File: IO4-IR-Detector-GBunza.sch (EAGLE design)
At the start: 45 parts, among them CON2 IO4INV, IC1 TL331, IC2 TL331, IC3 TL331, IC4 TL331, Q1 2N7002, Q2 2N7002, Q3 2N7002, Q4 2N7002

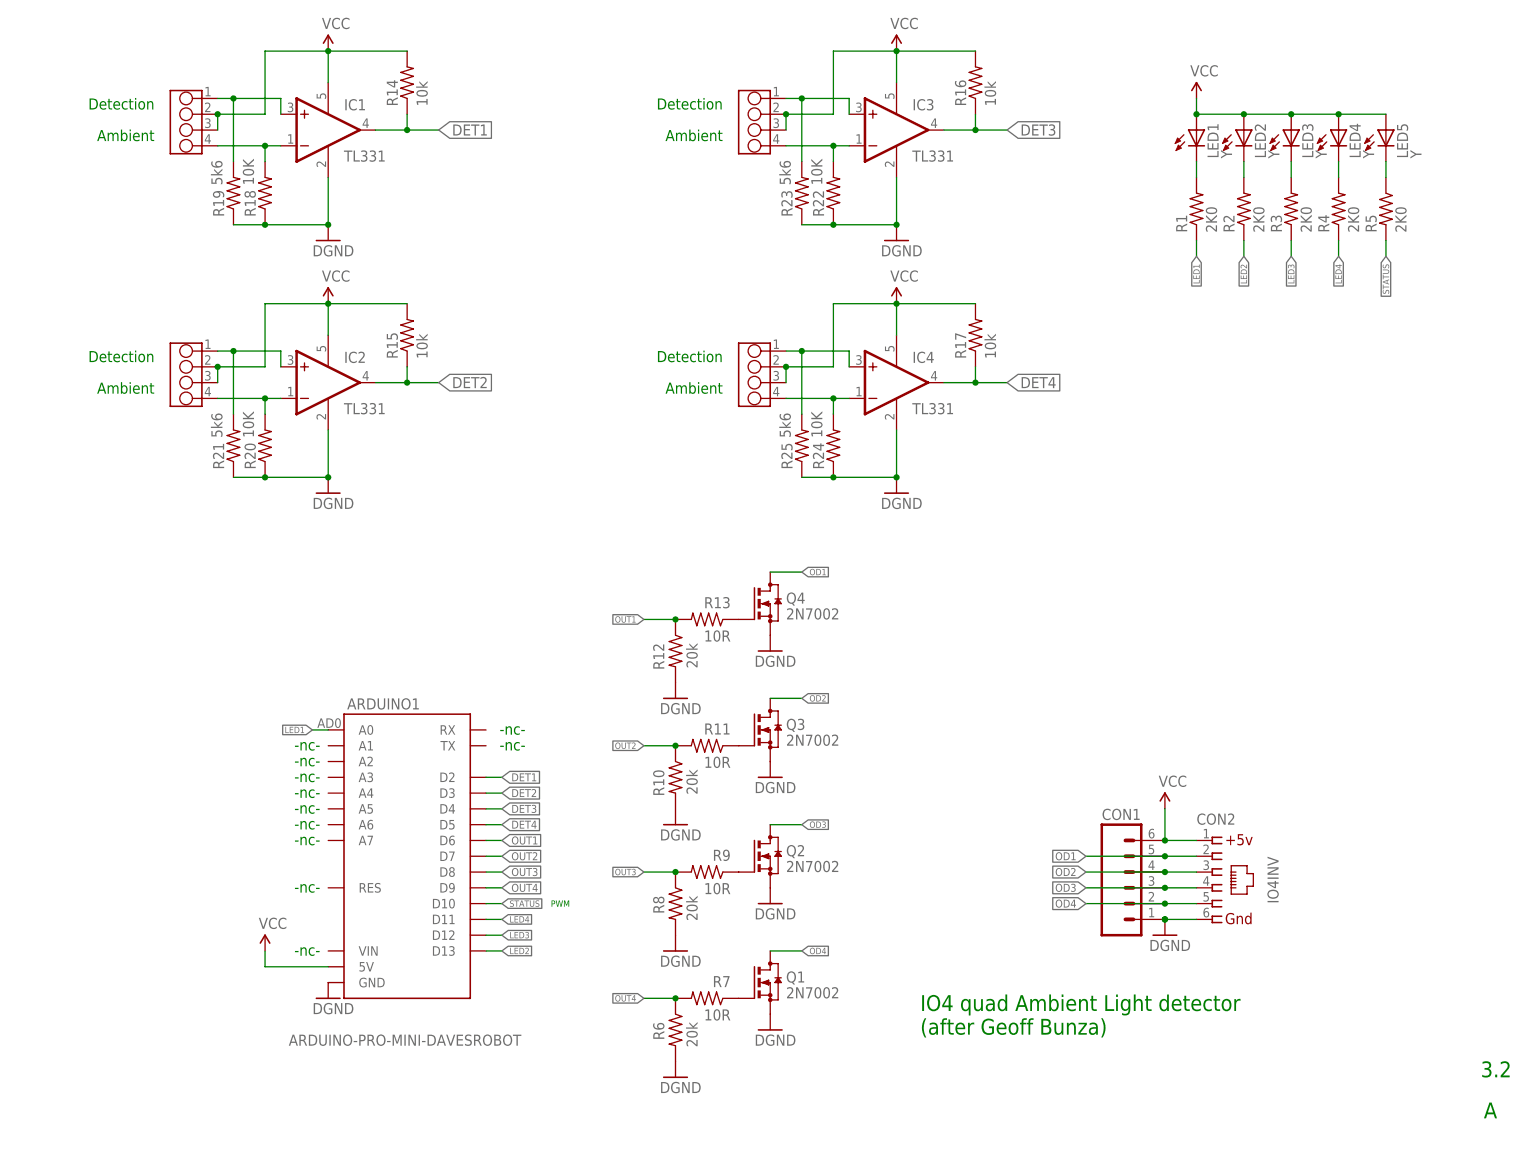
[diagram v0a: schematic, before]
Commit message: changed from expensive TL331 to inexpensive LM258/LM358
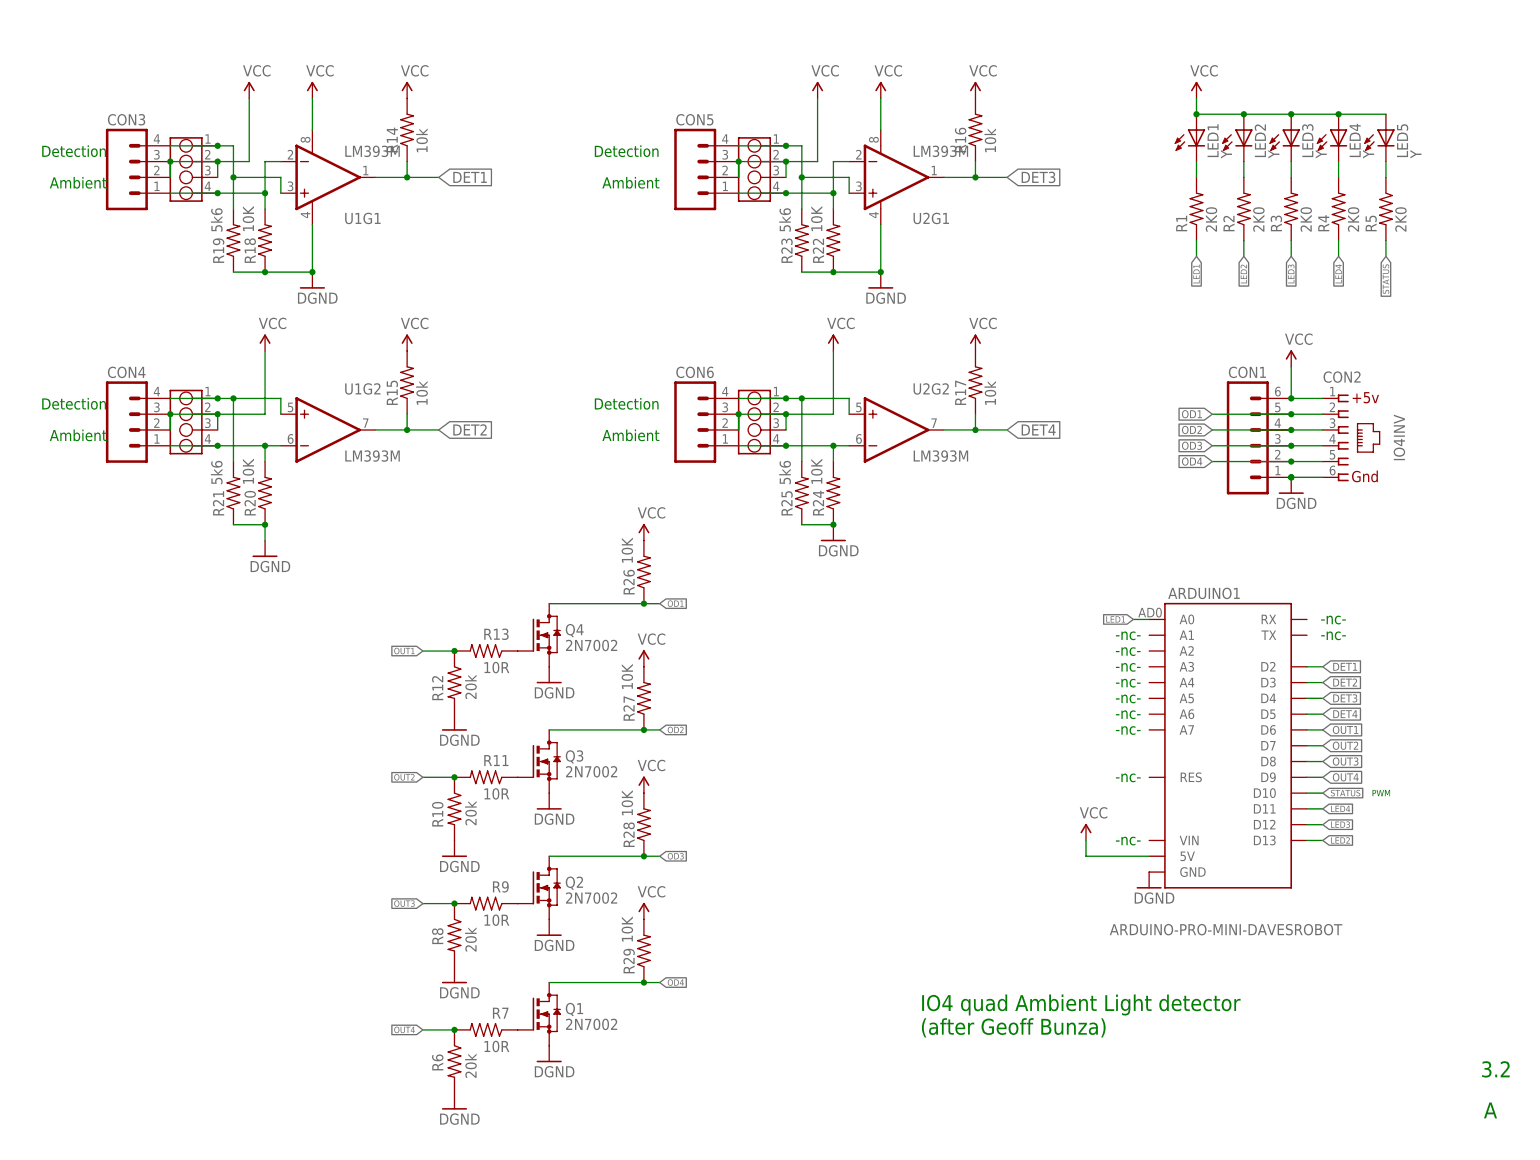
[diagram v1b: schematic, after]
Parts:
- removed IC1, IC2, IC3, IC4: TL331, SPCoast:TL331
- added CON3, CON4, CON5, CON6: (no value), SPCoast:CONNECTOR-M04LOCK
- added R26, R27, R28, R29: 10K, SPCoast:R0805-RES
- added U1, U2: LM393M, SPCoast:LM393M
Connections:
- net DET1: now also U1G1.OUT; no longer IC1.OUT
- net DET2: now also U1G2.OUT; no longer IC2.OUT
- net DET3: now also U2G1.OUT; no longer IC3.OUT
- net DET4: now also U2G2.OUT; no longer IC4.OUT
- net GND: now also U1G1.V-, U2G1.V-; no longer IC1.GND, IC2.GND, IC3.GND, IC4.GND
- net N$10: now also CON4.1, U1G2.-IN; no longer IC2.-IN
- net N$12: now also CON4.4, U1G2.+IN; no longer IC2.+IN
- net N$13: now also CON5.1, U2G1.-IN; no longer IC3.-IN
- net N$14: now also CON5.4, U2G1.+IN; no longer IC3.+IN
- net N$15: now also CON6.1, U2G2.-IN; no longer IC4.-IN
- net N$16: now also CON6.4, U2G2.+IN; no longer IC4.+IN
- net N$19: now also CON3.4, U1G1.+IN; no longer IC1.+IN
- net N$9: now also CON3.1, U1G1.-IN; no longer IC1.-IN
- net OD1: now also R26.1
- net OD2: now also R27.1
- net OD3: now also R28.1
- net OD4: now also R29.1
- net VCC: now also CON3.2, CON3.3, CON4.2, CON4.3, CON5.2, CON5.3, CON6.2, CON6.3, R26.2, R27.2, R28.2, R29.2, U1G1.V+, U2G1.V+; no longer IC1.V+, IC2.V+, IC3.V+, IC4.V+
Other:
- moved on the sheet: ARDUINO1, CON1, CON2, Q1, Q2, Q3, Q4, R10, R11, R12, R13, R14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

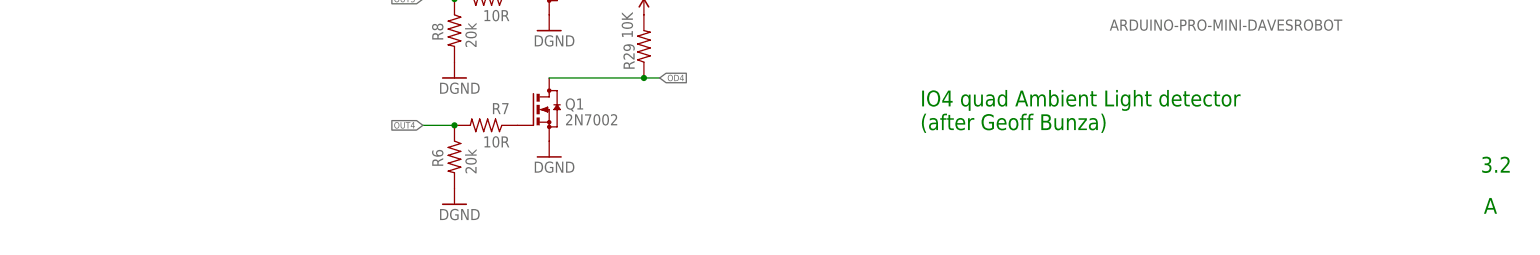
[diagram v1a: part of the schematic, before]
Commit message: added V4 changes note to sch
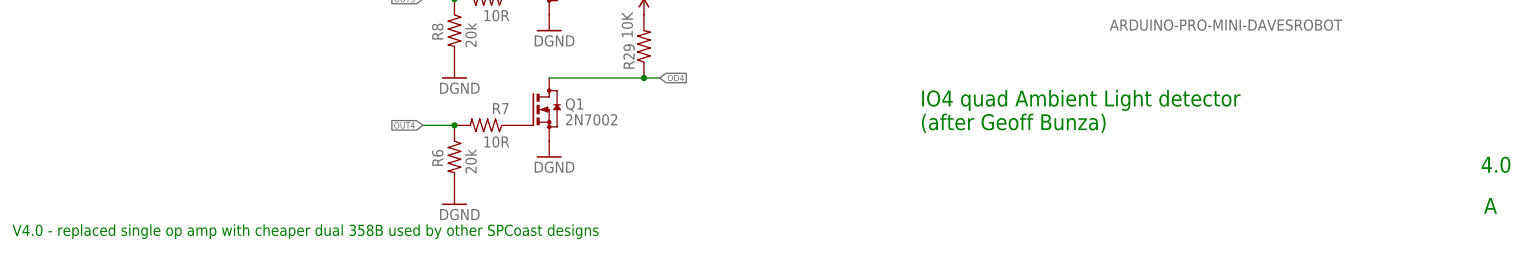
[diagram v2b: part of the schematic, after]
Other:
- note added: "4.0"
- note added: "V4.0 - replaced single op amp with cheaper dual 358B used by other SPCoast designs"
- note removed: "3.2"
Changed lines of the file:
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@@
 <text x="151.13" y="19.558" size="2.54" layer="91">IO4 quad Ambient Light detector
 (after Geoff Bunza)</text>
-<text x="241.3" y="12.7" size="2.54" layer="91">3.2</text>
+<text x="241.3" y="12.7" size="2.54" layer="91">4.0</text>
 <text x="241.808" y="6.096" size="2.54" layer="91">A</text>
 <text x="20.32" y="162.56" size="1.778" layer="91" rot="R180">Detection</text>
@@
 <text x="186.69" y="61.976" size="1.778" layer="91" rot="R180">-nc-</text>
 <text x="186.69" y="51.816" size="1.778" layer="91" rot="R180">-nc-</text>
+<text x="5.08" y="2.54" size="1.778" layer="91">V4.0 - replaced single op amp with cheaper dual 358B used by other SPCoast designs</text>
 </plain>
 <instances>

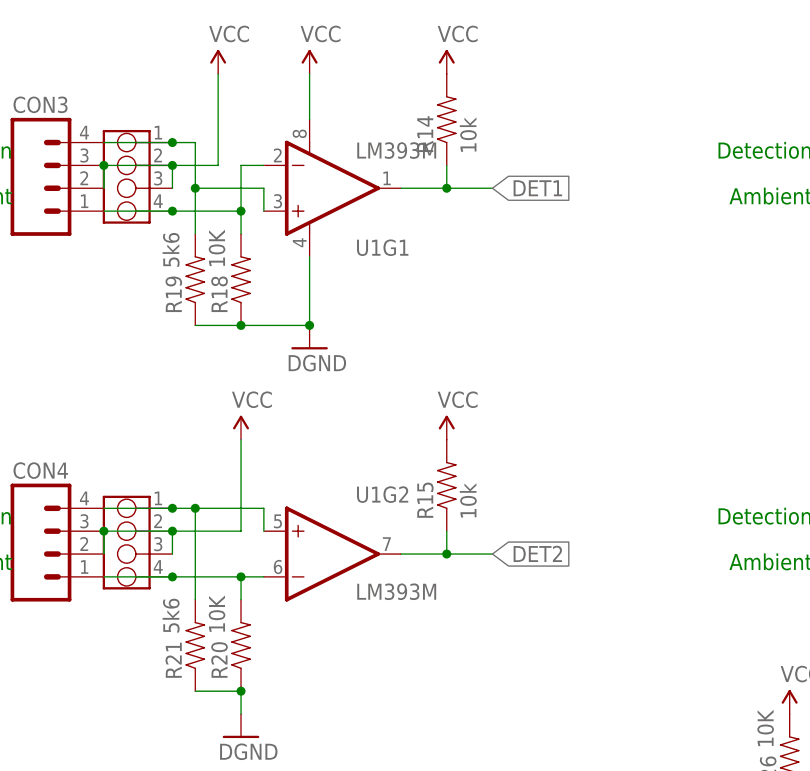
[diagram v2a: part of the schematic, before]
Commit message: op-amp value changed to LM358B
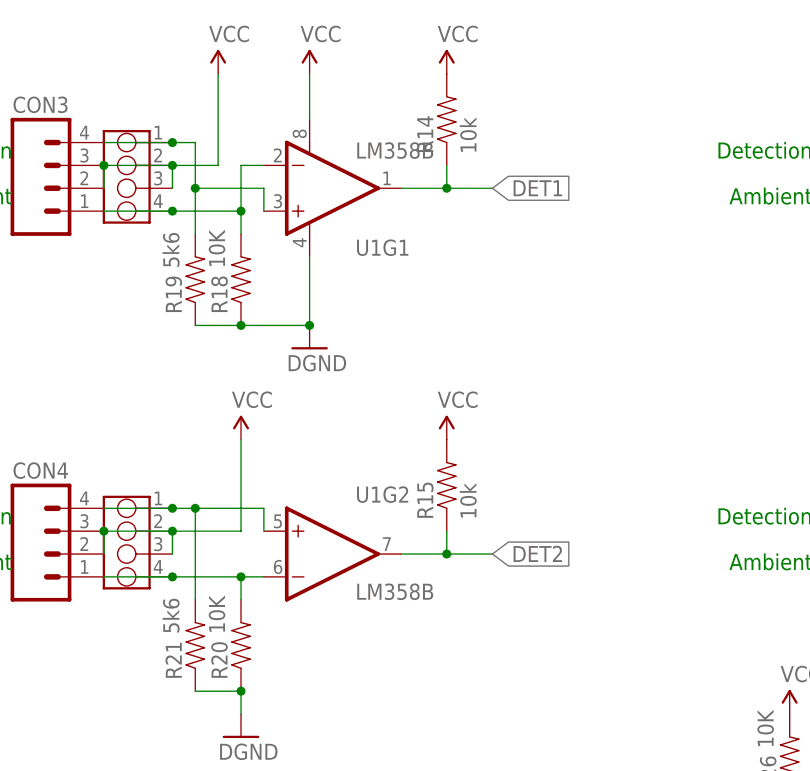
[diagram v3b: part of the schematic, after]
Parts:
- U1: value LM393M -> LM358B
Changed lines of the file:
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@@
 <part name="GND12" library="SparkFun-Aesthetics" deviceset="DGND" device=""/>
 <part name="GND14" library="SparkFun-Aesthetics" deviceset="DGND" device=""/>
-<part name="U1" library="SPCoast" deviceset="LM393" device="M"/>
+<part name="U1" library="SPCoast" deviceset="LM393" device="M" value="LM358B"/>
 <part name="U2" library="SPCoast" deviceset="LM393" device="M"/>
 <part name="SUPPLY8" library="SparkFun-Aesthetics" deviceset="VCC" device=""/>
